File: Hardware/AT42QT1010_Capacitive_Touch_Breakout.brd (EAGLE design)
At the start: 25.4 x 33 mm, 30 parts, among them Q1 NPN, U1 AT42QT1010UDFN

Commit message: Updated AT42QT Package description and Production ID.
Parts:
- U1: value AT42QT1010UDFN -> AT42QT1010 - UDFN
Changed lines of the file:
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@@
 </autorouter>
 <elements>
-<element name="U1" library="Testing" package="UDFN/USON_8_PAD" value="AT42QT1010UDFN" x="20.701" y="11.43" smashed="yes" rot="R180">
+<element name="U1" library="Testing" package="UDFN/USON_8_PAD" value="AT42QT1010 - UDFN" x="20.701" y="11.43" smashed="yes" rot="R180">
 <attribute name="NAME" x="18.796" y="13.335" size="0.4064" layer="25" rot="R270"/>
-<attribute name="VALUE" x="21.7535" y="11.4205" size="0.4064" layer="27" rot="R180"/>
+<attribute name="VALUE" value="AT42QT1010 - UDFN" x="21.7535" y="11.4205" size="0.4064" layer="27" rot="R180"/>
+<attribute name="PROD_ID" value="IC-13773" x="20.701" y="11.43" size="1.778" layer="27" rot="R180" display="off"/>
 </element>
 <element name="FRAME1" library="SparkFun-Aesthetics" package="CREATIVE_COMMONS" value="FRAME-LETTER" x="-15.24" y="-17.78"/>

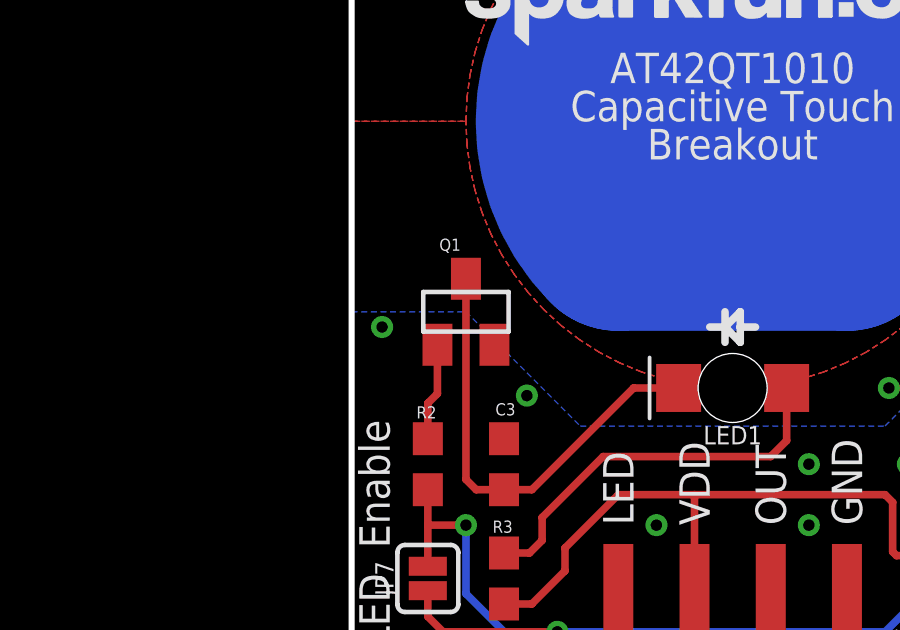
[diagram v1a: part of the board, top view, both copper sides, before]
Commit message: Moved new part to local library "local_parts" and updated transistor
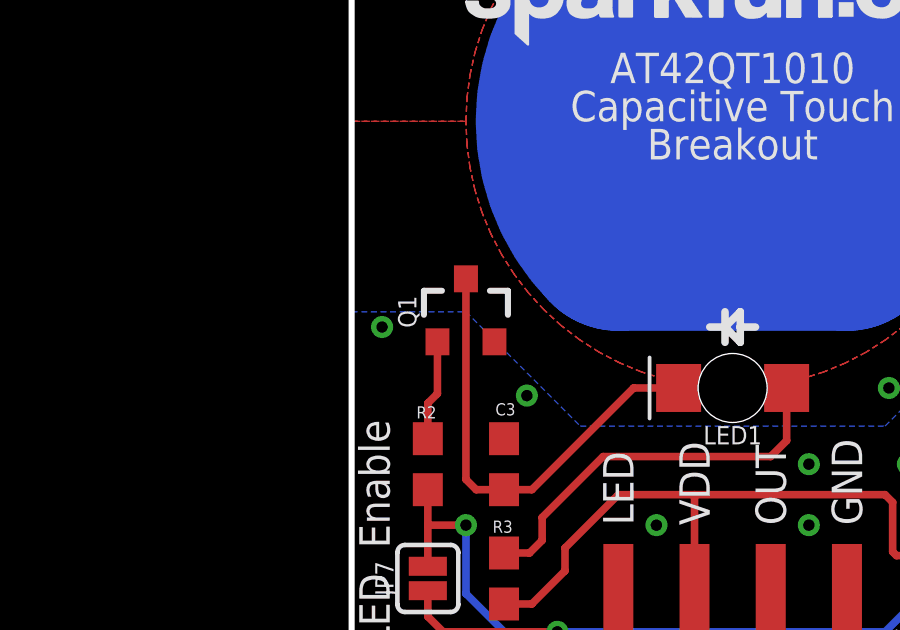
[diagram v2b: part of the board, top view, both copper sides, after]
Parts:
- Q1: value NPN -> 600mA/40V; device SparkFun-DiscreteSemi:SOT23 -> SparkFun-DiscreteSemi:SOT23-3
- U1: device Testing:UDFN/USON_8_PAD -> local_parts:UDFN/USON_8_PAD
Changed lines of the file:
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@@
 <layer number="47" name="Measures" color="7" fill="1" visible="no" active="yes"/>
 <layer number="48" name="Document" color="7" fill="1" visible="no" active="yes"/>
-<layer number="49" name="Reference" color="7" fill="1" visible="yes" active="yes"/>
+<layer number="49" name="Reference" color="7" fill="1" visible="no" active="yes"/>
 <layer number="50" name="dxf" color="7" fill="1" visible="no" active="yes"/>
 <layer number="53" name="tGND_GNDA" color="7" fill="9" visible="no" active="no"/>
@@
 </autorouter>
 <elements>
-<element name="U1" library="Testing" package="UDFN/USON_8_PAD" value="AT42QT1010 - UDFN" x="20.701" y="11.43" smashed="yes" rot="R180">
+<element name="U1" library="local_parts" package="UDFN/USON_8_PAD" value="AT42QT1010 - UDFN" x="20.701" y="11.43" smashed="yes" rot="R180">
 <attribute name="NAME" x="18.796" y="13.335" size="0.4064" layer="25" rot="R270"/>
 <attribute name="VALUE" value="AT42QT1010 - UDFN" x="21.7535" y="11.4205" size="0.4064" layer="27" rot="R180"/>
@@
 <attribute name="PROD_ID" value="RES-08220" x="5.08" y="7.62" size="1.778" layer="27" rot="R270" display="off"/>
 </element>
-<element name="Q1" library="SparkFun-DiscreteSemi" package="SOT23" value="NPN" x="3.81" y="16.51">
+<element name="Q1" library="SparkFun-DiscreteSemi" package="SOT23-3" value="600mA/40V" x="3.81" y="16.51">
 <attribute name="PROD_ID" value="TRANS-08049" x="19.05" y="-7.62" size="1.778" layer="27" display="off"/>
-<attribute name="VALUE" value="MMBT2222A" x="19.05" y="-7.62" size="1.778" layer="27" display="off"/>
+<attribute name="VALUE" value="600mA/40V" x="19.05" y="-7.62" size="1.778" layer="27" display="off"/>
 </element>
 <element name="STANDOFF1" library="SparkFun-Electromechanical" package="STAND-OFF" value="STAND-OFF" x="22.86" y="2.54"/>
@@
 <wire x1="2.54" y1="12.28" x2="2.54" y2="13.462" width="0.254" layer="1"/>
 <wire x1="2.54" y1="13.462" x2="2.86" y2="13.782" width="0.254" layer="1"/>
-<wire x1="2.86" y1="15.41" x2="2.86" y2="13.782" width="0.254" layer="1"/>
+<wire x1="2.86" y1="15.51" x2="2.86" y2="13.782" width="0.254" layer="1"/>
 </signal>
 <signal name="N$11">

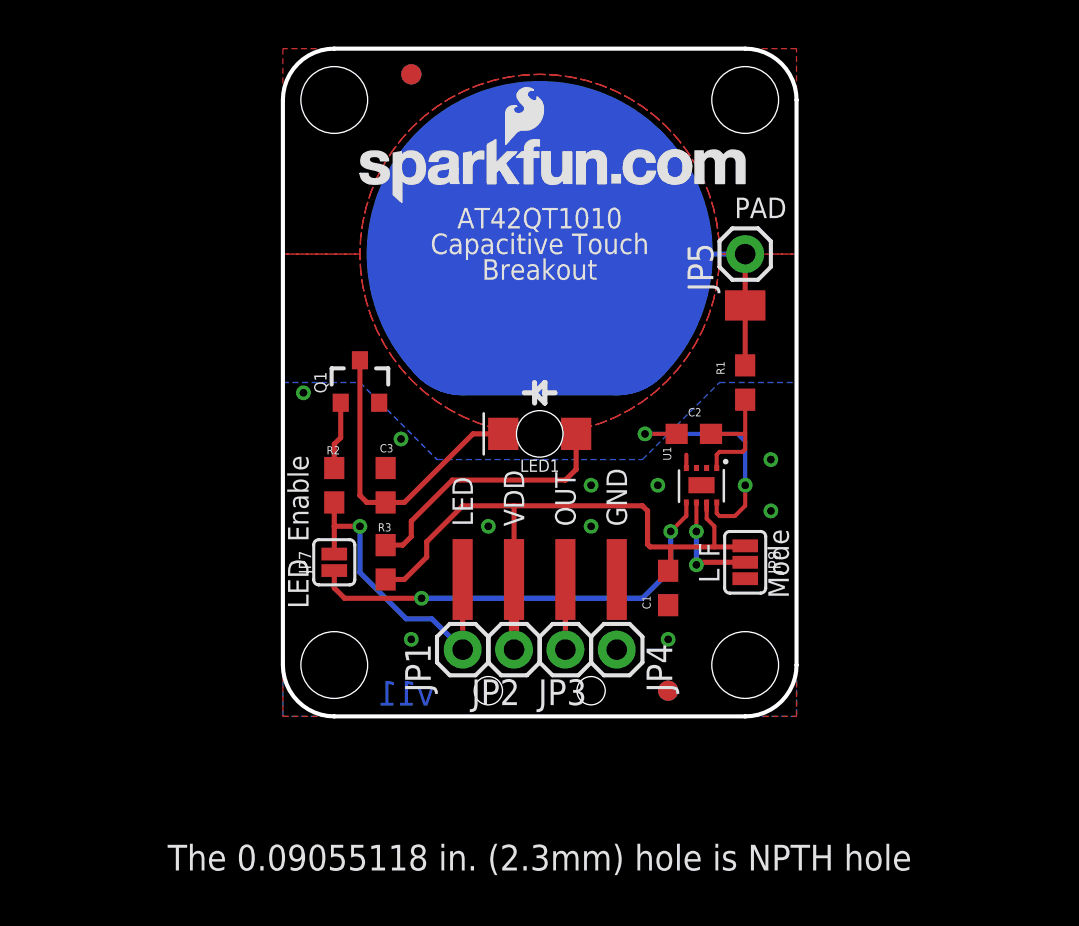
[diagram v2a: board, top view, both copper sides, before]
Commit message: Fixed issues from double check
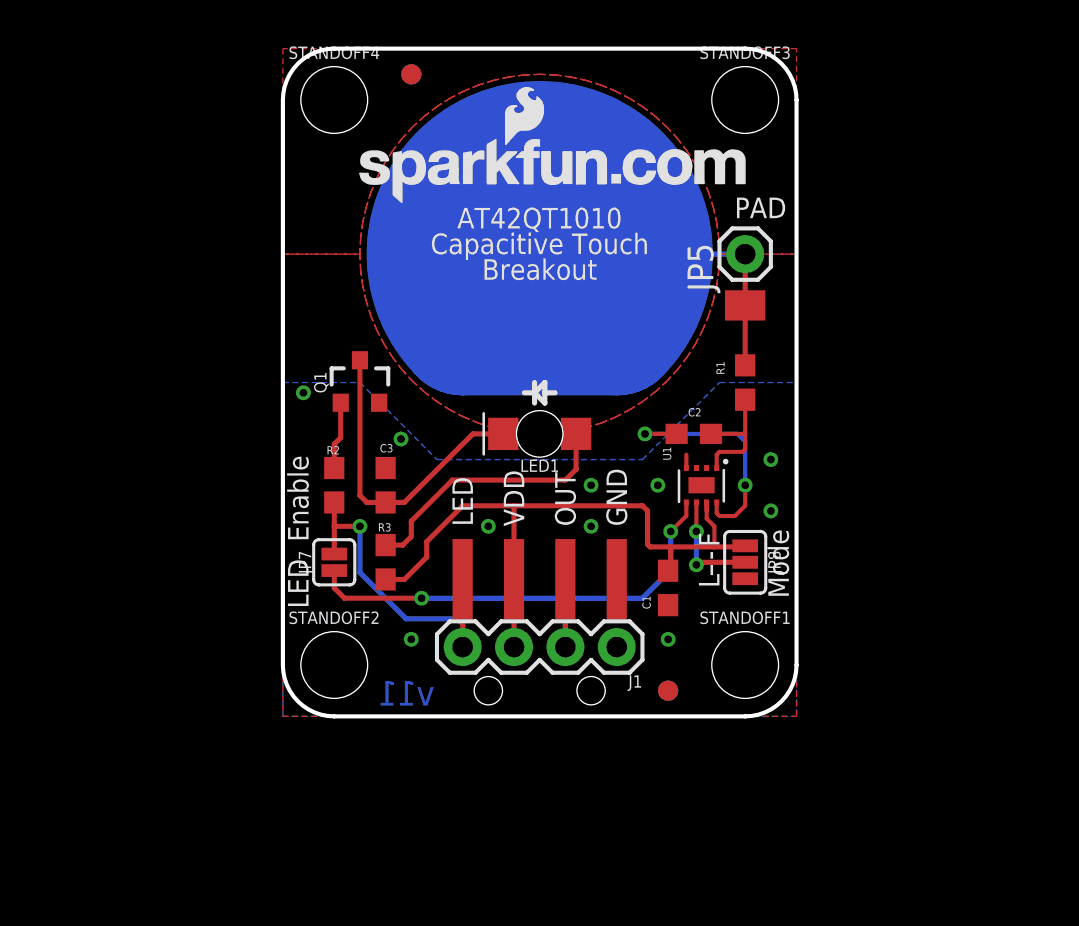
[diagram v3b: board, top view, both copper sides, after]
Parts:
- removed JP1, JP2, JP3, JP4: M01PTH, SparkFun-Connectors:1X01
- added J1: (no value), SparkFun-Connectors:1X04
- added U$1: SPECIAL_INSTRUCTIONS-ORDERING, SparkFun-Aesthetics:ORDERING_INSTRUCTIONS
- JP5: value M01PTH -> (none)
- JP6: device SparkFun-Connectors:1X04-SMD_LONG -> SparkFun-Connectors:1X04_SMD_LONG
- LOGO1: value SFE_LOGO_FLAME.3_INCH -> SFE_LOGO_FLAME0.05_INCH; device SparkFun-Aesthetics:SFE_LOGO_FLAME_.3 -> SparkFun-Aesthetics:SFE_LOGO_FLAME_.05
- STANDOFF1, STANDOFF2, STANDOFF3, STANDOFF4: device SparkFun-Electromechanical:STAND-OFF -> SparkFun-Hardware:STAND-OFF
- moved LOGO1 12.5 mm to (2.79, 18.4)
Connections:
- net GND: now also J1.1; no longer JP4.1
- net LED: now also J1.4; no longer JP1.1
- net OUT: now also J1.2; no longer JP3.1
- net VCC: now also J1.3; no longer JP2.1
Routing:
- net LED: track 16.2 -> 17.1 mm
- net OUT: track 28.0 -> 28.6 mm
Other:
- board text removed: "typ."

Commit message: Made space for and added version jumpers
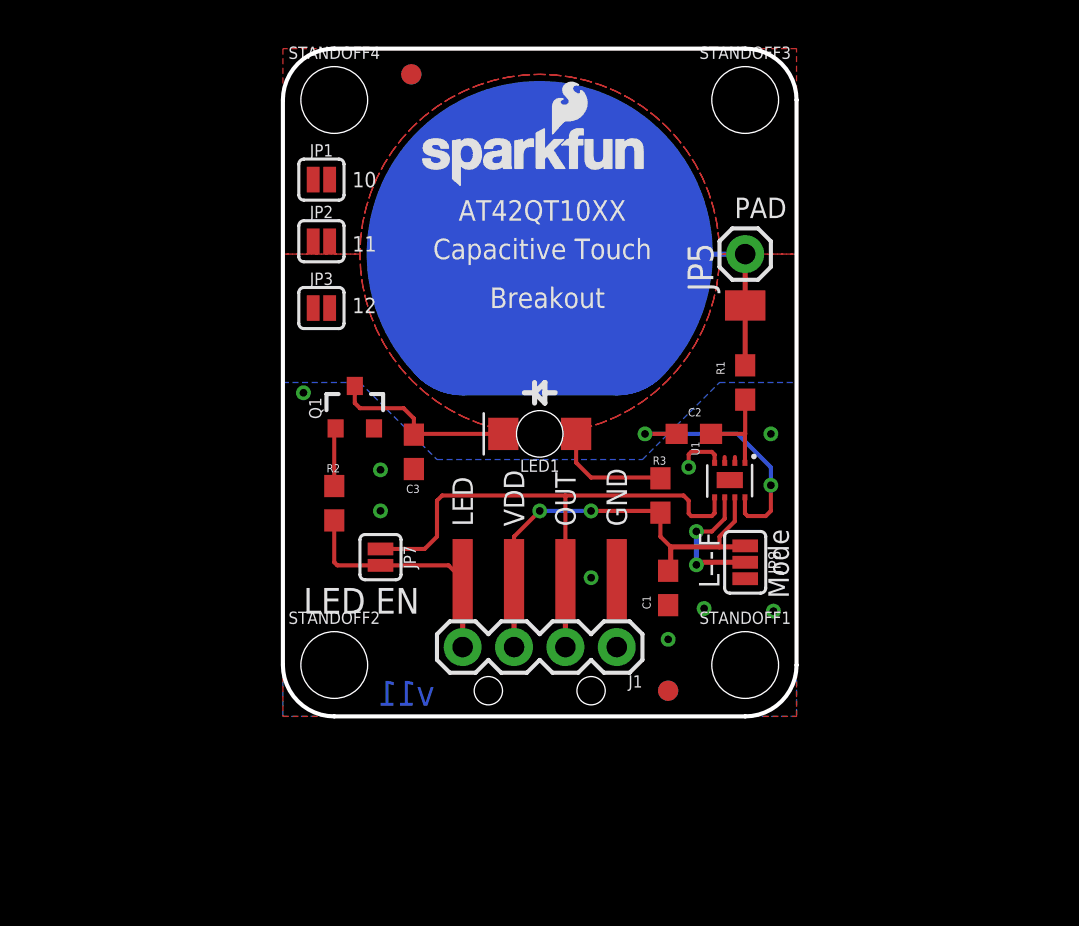
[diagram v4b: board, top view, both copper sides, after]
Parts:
- removed LOGO1: SFE_LOGO_FLAME0.05_INCH, SparkFun-Aesthetics:SFE_LOGO_FLAME_.05
- removed LOGO5: SFE_LOGO_NAME_WEB, SparkFun-Aesthetics:SFE_LOGO_NAME_WEB
- added JP1: JUMPER-SMT_2_NC_PASTE_SILK, SparkFun-Jumpers:SMT-JUMPER_2_NC_PASTE_SILK
- added JP2, JP3: JUMPER-SMT_2_NO_SILK, SparkFun-Jumpers:SMT-JUMPER_2_NO_SILK
- added LOGO3: SFE_LOGO_NAME_FLAME.1_INCH, SparkFun-Aesthetics:SFE_LOGO_NAME_FLAME_.1
- added LOGO4: SFE_LOGO_FLAME.2_INCH, SparkFun-Aesthetics:SFE_LOGO_FLAME_.2
- moved R3 14.0 mm to (18.7, 10.9)
- moved JP7 2.30 mm to (4.83, 7.87), turned to 270 degrees
- moved C3 2.16 mm to (6.48, 13.1), turned to 270 degrees
- moved U1 1.42 mm to (22.1, 11.7)
- moved Q1 1.30 mm to (3.56, 15.2)
- moved R2 0.89 mm to (2.54, 10.5)
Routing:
- net VCC: track 32.6 -> 22.9 mm, vias 0 -> 2
- net N$12: track 13.2 -> 5.95 mm
- net N$11: track 15.3 -> 9.32 mm
- net LED: track 17.1 -> 13.1 mm, vias 1 -> 0
- net GND: track 0.66 -> 2.43 mm, vias 10 -> 9
- net N$5: track 6.32 -> 4.82 mm
- net N$7: track 5.55 -> 6.83 mm
- net N$4: track 12.1 -> 12.9 mm
- net OUT: track 28.6 -> 27.8 mm, vias 2 -> 0
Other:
- board text added: "10"
- board text added: "11"
- board text added: "12"
- board text added: "AT42QT10XX"
- board text added: "LED EN"
- board text removed: "AT42QT1010"
- board text removed: "Enable"

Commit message: Revert "Made space for and added version jumpers"
This reverts commit 0dfcf3fd33d472c1ea0c54a853371dbd5ffd3b83.
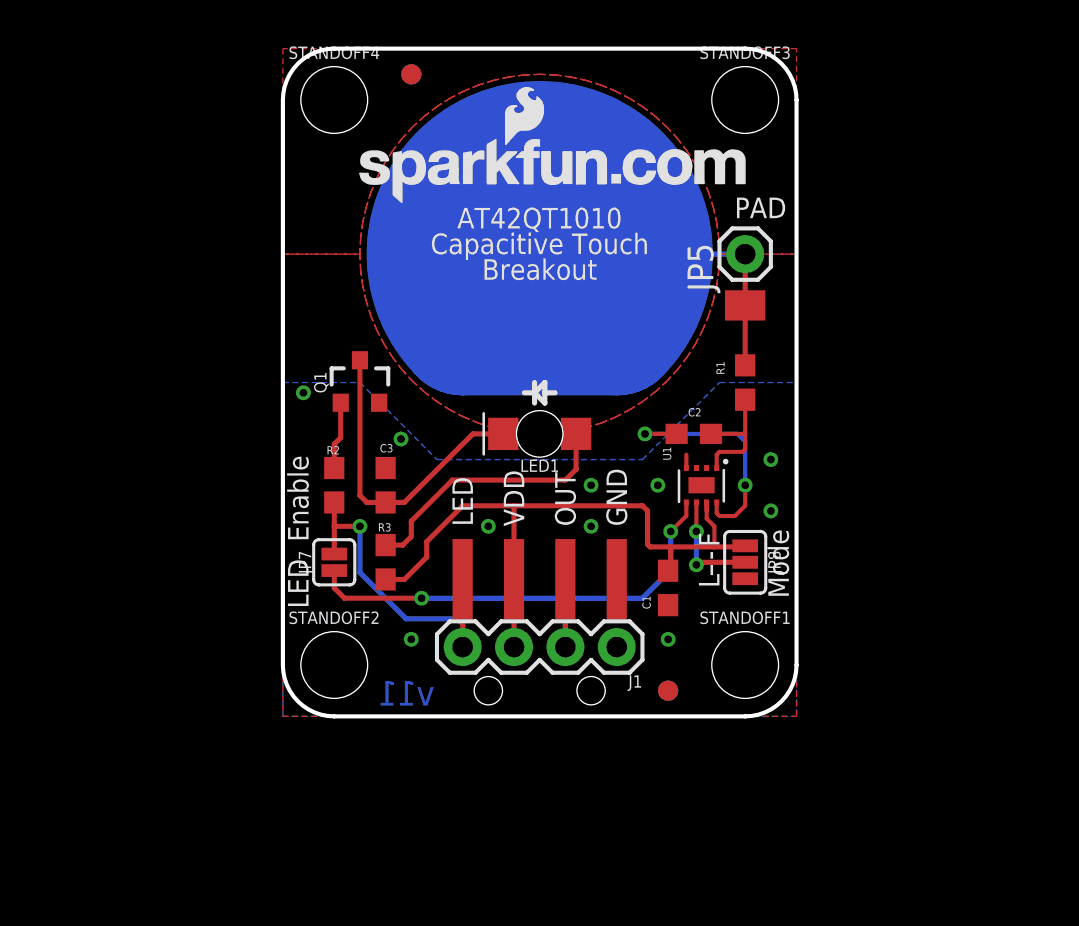
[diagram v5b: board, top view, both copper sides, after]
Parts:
- removed JP1: JUMPER-SMT_2_NC_PASTE_SILK, SparkFun-Jumpers:SMT-JUMPER_2_NC_PASTE_SILK
- removed JP2, JP3: JUMPER-SMT_2_NO_SILK, SparkFun-Jumpers:SMT-JUMPER_2_NO_SILK
- removed LOGO3: SFE_LOGO_NAME_FLAME.1_INCH, SparkFun-Aesthetics:SFE_LOGO_NAME_FLAME_.1
- removed LOGO4: SFE_LOGO_FLAME.2_INCH, SparkFun-Aesthetics:SFE_LOGO_FLAME_.2
- added LOGO1: SFE_LOGO_FLAME0.05_INCH, SparkFun-Aesthetics:SFE_LOGO_FLAME_.05
- added LOGO5: SFE_LOGO_NAME_WEB, SparkFun-Aesthetics:SFE_LOGO_NAME_WEB
- moved R3 14.0 mm to (5.08, 7.62)
- moved JP7 2.30 mm to (2.54, 7.62), turned to 90 degrees
- moved C3 2.16 mm to (5.08, 11.4), turned to 90 degrees
- moved U1 1.42 mm to (20.7, 11.4)
- moved Q1 1.30 mm to (3.81, 16.5)
- moved R2 0.89 mm to (2.54, 11.4)
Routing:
- net VCC: track 22.9 -> 32.6 mm, vias 2 -> 0
- net N$12: track 5.95 -> 13.2 mm
- net N$11: track 9.32 -> 15.3 mm
- net LED: track 13.1 -> 17.1 mm, vias 0 -> 1
- net GND: track 2.43 -> 0.66 mm, vias 9 -> 10
- net N$5: track 4.82 -> 6.32 mm
- net N$7: track 6.83 -> 5.55 mm
- net N$4: track 12.9 -> 12.1 mm
- net OUT: track 27.8 -> 28.6 mm, vias 0 -> 2
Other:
- board text added: "AT42QT1010"
- board text added: "Enable"
- board text removed: "10"
- board text removed: "11"
- board text removed: "12"
- board text removed: "AT42QT10XX"
- board text removed: "LED EN"

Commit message: New branch due to the large changes to the existing direction of the product
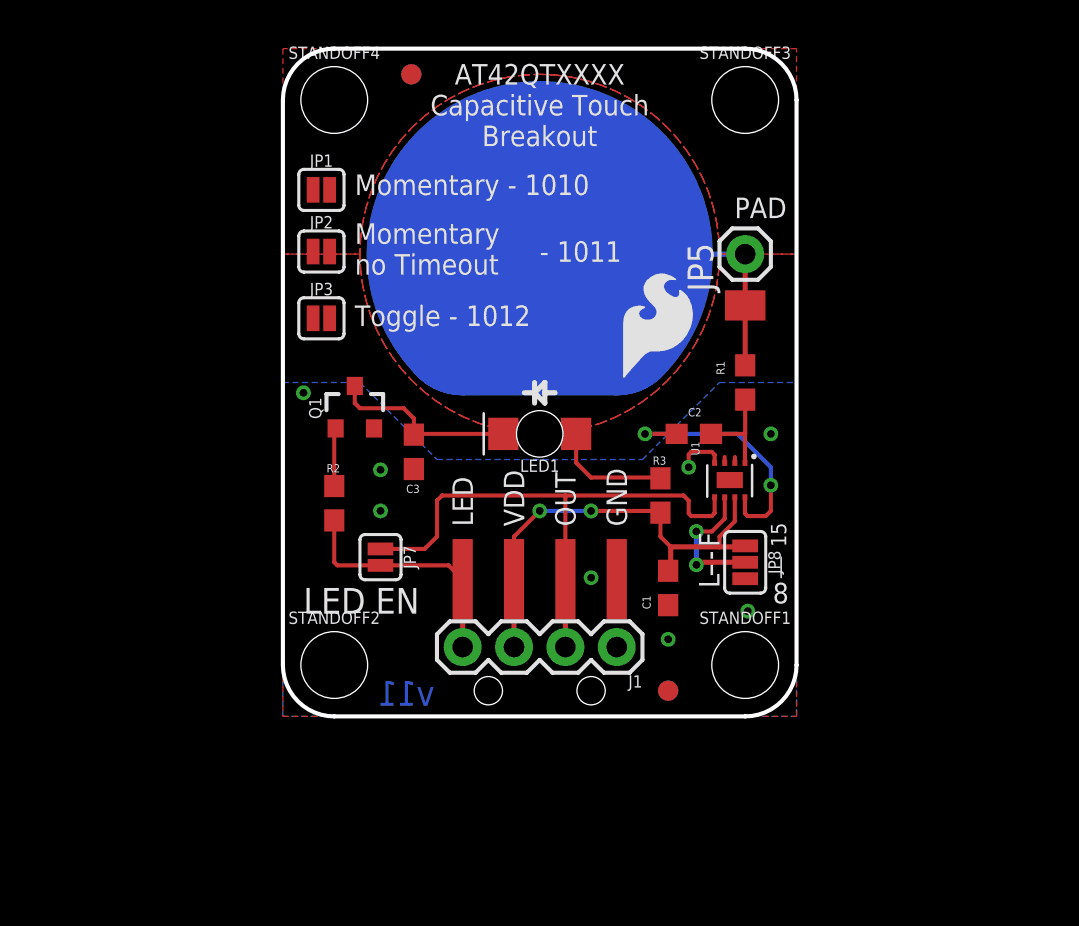
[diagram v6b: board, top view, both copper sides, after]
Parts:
- removed LOGO5: SFE_LOGO_NAME_WEB, SparkFun-Aesthetics:SFE_LOGO_NAME_WEB
- added JP1, JP2, JP3: JUMPER-SMT_2_NO_SILK, SparkFun-Jumpers:SMT-JUMPER_2_NO_SILK
- added LOGO4: SFE_LOGO_FLAME.2_INCH, SparkFun-Aesthetics:SFE_LOGO_FLAME_.2
- LOGO1: value SFE_LOGO_FLAME0.05_INCH -> SFE_LOGO_FLAME.2_INCH; device SparkFun-Aesthetics:SFE_LOGO_FLAME_.05 -> SparkFun-Aesthetics:SFE_LOGO_FLAME_.2
- moved R3 14.0 mm to (18.7, 10.9)
- moved LOGO1 13.8 mm to (16.5, 16.5), flipped to the top
- moved JP7 2.30 mm to (4.83, 7.87), turned to 270 degrees
- moved C3 2.16 mm to (6.48, 13.1), turned to 270 degrees
- moved U1 1.42 mm to (22.1, 11.7)
- moved Q1 1.30 mm to (3.56, 15.2)
- moved R2 0.89 mm to (2.54, 10.5)
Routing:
- net VCC: track 32.6 -> 22.9 mm, vias 0 -> 2
- net N$12: track 13.2 -> 5.95 mm
- net N$11: track 15.3 -> 9.32 mm
- net LED: track 17.1 -> 13.1 mm, vias 1 -> 0
- net GND: track 0.66 -> 2.43 mm, vias 10 -> 8
- net N$5: track 6.32 -> 4.82 mm
- net N$7: track 5.55 -> 6.83 mm
- net N$4: track 12.1 -> 12.9 mm
- net OUT: track 28.6 -> 27.8 mm, vias 2 -> 0
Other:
- board text added: "- 1011"
- board text added: "15"
- board text added: "8"
- board text added: "AT42QTXXXX Capacitive Touch Breakout"
- board text added: "LED EN"
- board text added: "Momentary - 1010"
- board text added: "Momentary no Timeout"
- board text added: "Toggle - 1012"
- board text removed: "AT42QT1010"
- board text removed: "Breakout"
- board text removed: "Capacitive Touch"
- board text removed: "Enable"
- board text removed: "Mode"
